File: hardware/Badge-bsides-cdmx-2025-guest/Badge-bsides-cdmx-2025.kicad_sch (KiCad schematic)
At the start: 30 parts, among them J1 SWDIO, J3 ADDON, J4 Conn_01x04_Pin, J5 I2C, J6 Conn_01x04_Pin, P6 USB_C_Plug_USB2.0, Q3 DMG3415U-7, SW11 ON, SW2 RESET, U1 PY32F030F28U6TR, U6 AP2112K-3.3

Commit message: feat(Hw):started_routing
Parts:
- added C67, C68, C69, C70: 10uF, Capacitor_SMD:C_0603_1608Metric, symbol Device:C_Small
- added R5, R6, R7, R8: 10k, Resistor_SMD:R_0603_1608Metric, symbol Device:R_Small
- added SW10, SW7, SW8, SW9: SW_Push, Footprints:TS1088R02026, symbol Switch:SW_Push
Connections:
- net +3.3V: no longer BT3.2 (+)
- net +3V3: now also R5.2, R6.2, R7.2, R8.2
- net +BATT: now also BT3.2 (+)
- net GND: now also C67.2, C68.2, C69.2, C70.2, SW10.1, SW7.1, SW8.1, SW9.1
- net GPIO1: now also J3.6 (Pin_6), U1.3 (PA7); no longer J3.5 (Pin_5), U1.17 (PA1)
- net GPIO2: now also J3.5 (Pin_5), U1.5 (PA12); no longer J3.6 (Pin_6), U1.16 (PA0)
- net LED1: now also U1.10 (PB6); no longer U1.2 (PA6)
- net LED2: now also U1.20 (PA4); no longer U1.3 (PA7)
- net BTTN2: now reaches U1.1 (PA5)
- net BTTN2: now also C68.1, R6.1, SW9.2
- new net BTTN1: C67.1, R5.1, SW8.2, U1.2 (PA6)
- new net BTTN3: C69.1, R7.1, SW7.2, U1.17 (PA1)
- new net BTTN4: C70.1, R8.1, SW10.2, U1.16 (PA0)
- no-connect marks 9 -> 3
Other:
- moved on the sheet: BT3, BT4

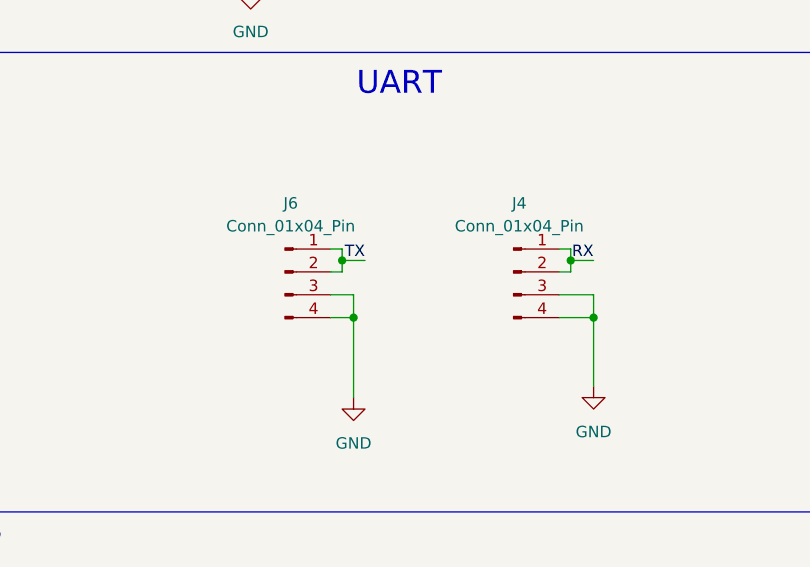
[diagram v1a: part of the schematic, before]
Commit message: feat(Hw):Route_Sponsor
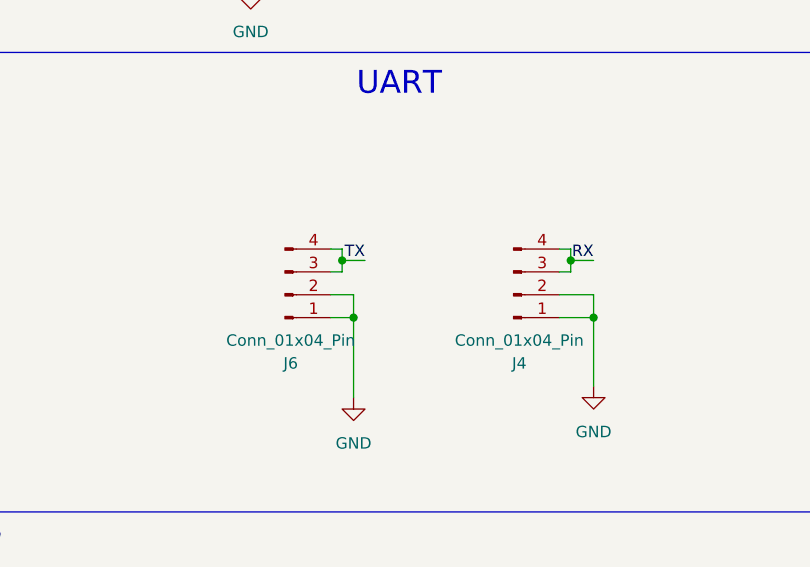
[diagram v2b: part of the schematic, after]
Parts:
- J4: footprint Connector_PinHeader_2.54mm:PinHeader_1x04_P2.54mm_Vertical -> Connector_PinHeader_2.54mm:PinHeader_1x04_P2.54mm_Horizontal
- J6: footprint Connector_PinHeader_2.54mm:PinHeader_1x04_P2.54mm_Vertical -> Connector_PinSocket_2.54mm:PinSocket_1x04_P2.54mm_Horizontal
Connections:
- net GND: now also J4.1 (Pin_1), J4.2 (Pin_2), J6.1 (Pin_1), J6.2 (Pin_2); no longer J4.3 (Pin_3), J4.4 (Pin_4), J6.3 (Pin_3), J6.4 (Pin_4)
- net RX: now also J4.3 (Pin_3), J4.4 (Pin_4); no longer J4.1 (Pin_1), J4.2 (Pin_2)
- net TX: now also J6.3 (Pin_3), J6.4 (Pin_4); no longer J6.1 (Pin_1), J6.2 (Pin_2)
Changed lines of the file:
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@@
 	(symbol
 		(lib_id "Connector:Conn_01x04_Pin")
-		(at 246.38 93.98 0)
-		(unit 1)
-		(exclude_from_sim no)
-		(in_bom yes)
-		(on_board yes)
-		(dnp no)
-		(fields_autoplaced yes)
+		(at 246.38 96.52 0)
+		(mirror x)
+		(unit 1)
+		(exclude_from_sim no)
+		(in_bom yes)
+		(on_board yes)
+		(dnp no)
 		(property "Reference" "J4"
-			(at 247.015 86.36 0)
+			(at 247.015 104.14 0)
 			(effects
 				(font
@@
 		)
 		(property "Value" "Conn_01x04_Pin"
-			(at 247.015 88.9 0)
-			(effects
-				(font
-					(size 1.27 1.27)
-				)
-			)
-		)
-		(property "Footprint" "Connector_PinHeader_2.54mm:PinHeader_1x04_P2.54mm_Vertical"
-			(at 246.38 93.98 0)
+			(at 247.015 101.6 0)
+			(effects
+				(font
+					(size 1.27 1.27)
+				)
+			)
+		)
+		(property "Footprint" "Connector_PinHeader_2.54mm:PinHeader_1x04_P2.54mm_Horizontal"
+			(at 246.38 96.52 0)
 			(effects
 				(font
@@
 		)
 		(property "Datasheet" "~"
-			(at 246.38 93.98 0)
+			(at 246.38 96.52 0)
 			(effects
 				(font
@@
 		)
 		(property "Description" "Generic connector, single row, 01x04, script generated"
-			(at 246.38 93.98 0)
+			(at 246.38 96.52 0)
 			(effects
 				(font
@@
 	(symbol
 		(lib_id "Connector:Conn_01x04_Pin")
-		(at 220.98 93.98 0)
-		(unit 1)
-		(exclude_from_sim no)
-		(in_bom yes)
-		(on_board yes)
-		(dnp no)
-		(fields_autoplaced yes)
+		(at 220.98 96.52 0)
+		(mirror x)
+		(unit 1)
+		(exclude_from_sim no)
+		(in_bom yes)
+		(on_board yes)
+		(dnp no)
 		(property "Reference" "J6"
-			(at 221.615 86.36 0)
+			(at 221.615 104.14 0)
 			(effects
 				(font
@@
 		)
 		(property "Value" "Conn_01x04_Pin"
-			(at 221.615 88.9 0)
-			(effects
-				(font
-					(size 1.27 1.27)
-				)
-			)
-		)
-		(property "Footprint" "Connector_PinHeader_2.54mm:PinHeader_1x04_P2.54mm_Vertical"
-			(at 220.98 93.98 0)
+			(at 221.615 101.6 0)
+			(effects
+				(font
+					(size 1.27 1.27)
+				)
+			)
+		)
+		(property "Footprint" "Connector_PinSocket_2.54mm:PinSocket_1x04_P2.54mm_Horizontal"
+			(at 220.98 96.52 0)
 			(effects
 				(font
@@
 		)
 		(property "Datasheet" "~"
-			(at 220.98 93.98 0)
+			(at 220.98 96.52 0)
 			(effects
 				(font
@@
 		)
 		(property "Description" "Generic connector, single row, 01x04, script generated"
-			(at 220.98 93.98 0)
-			(effects
-				(font
+			(at 220.98 96.52 0)
+			(effects
+				(font

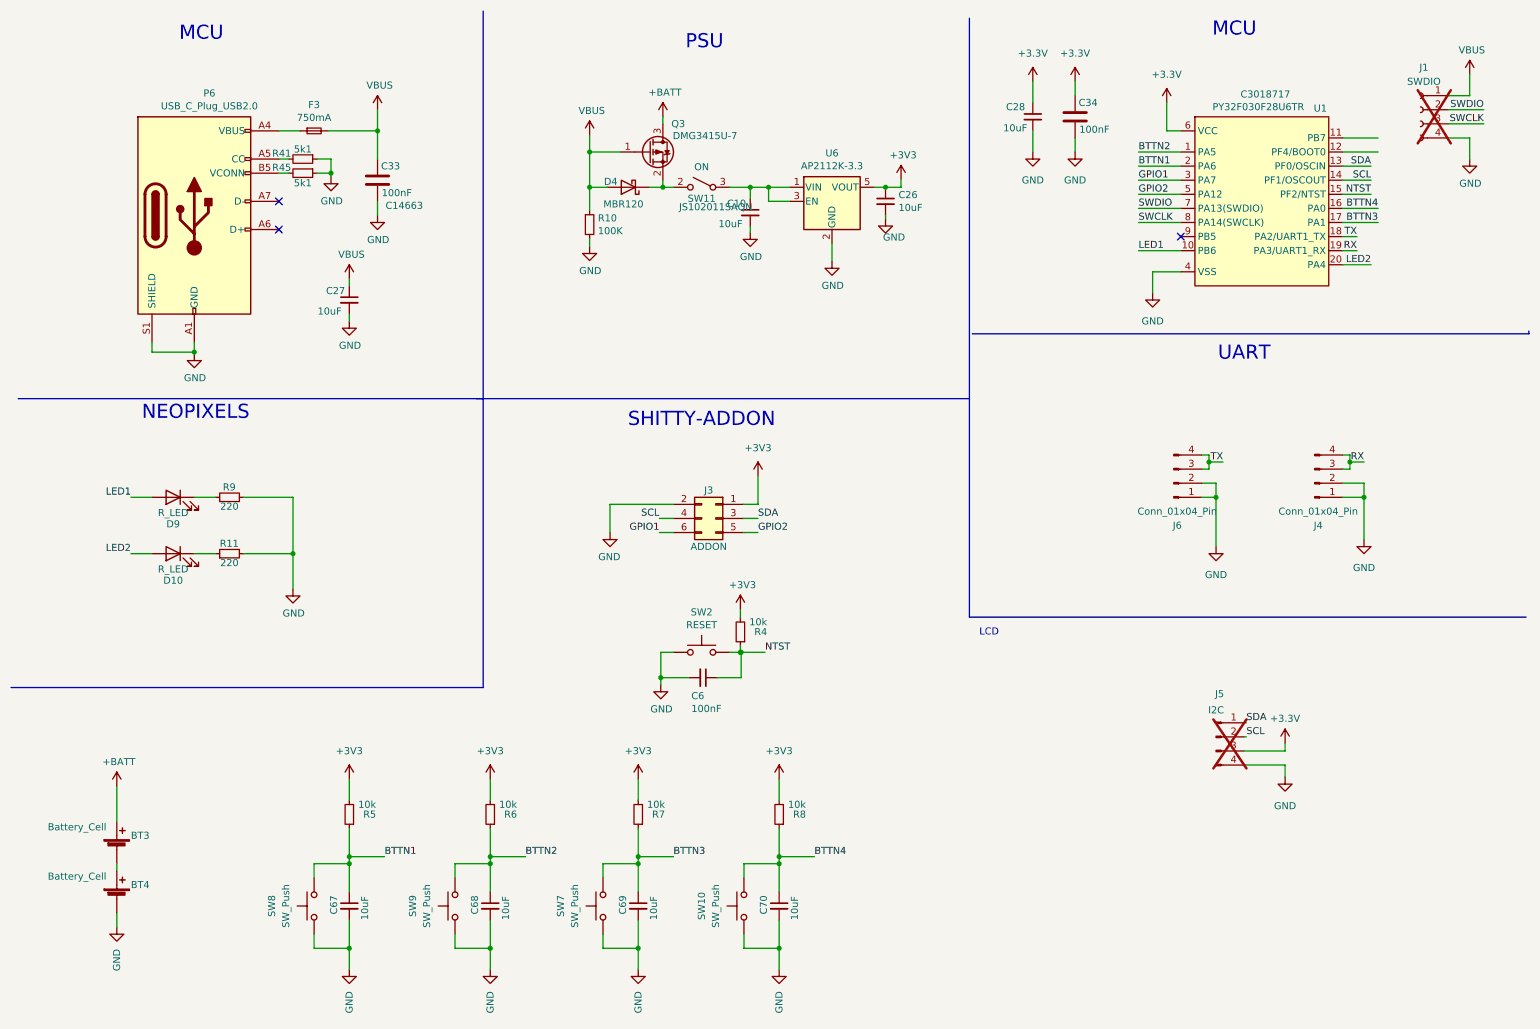
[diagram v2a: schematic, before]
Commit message: feat(Hw):Neopixels_added(sponsor)
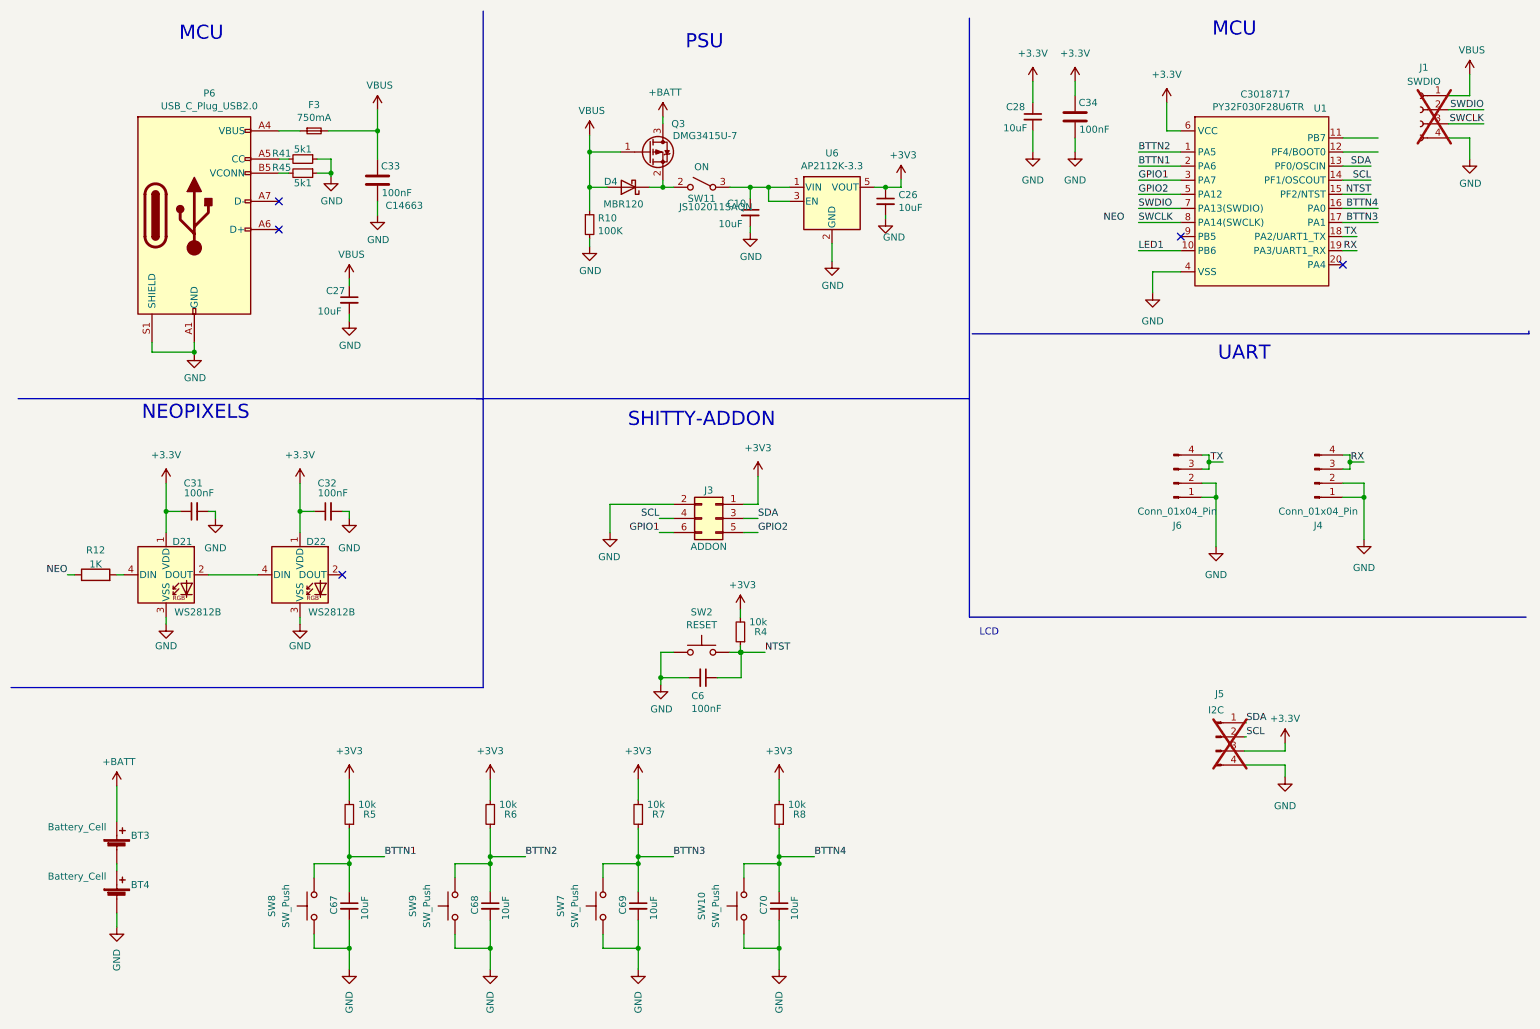
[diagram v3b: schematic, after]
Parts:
- removed D10, D9: R_LED, Footprints:LYT77K-K2M1, symbol Device:LED
- removed R11, R9: 220, Resistor_SMD:R_0603_1608Metric, symbol Device:R_Small
- added C31, C32: 100nF, Capacitor_SMD:C_0603_1608Metric, symbol Device:C_Small
- added D21, D22: WS2812B, Footprints:LED_SK6812-E, symbol LED:WS2812B
- added R12: 1K, Resistor_SMD:R_0603_1608Metric, symbol Device:R
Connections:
- net +3.3V: now also C31.1, C32.1, D21.1 (VDD), D22.1 (VDD)
- net GND: now also C31.2, C32.2, D21.3 (VSS), D22.3 (VSS)
- net LED2: no longer names the net of U1.20 (PA4)
- new net: D21.2 (DOUT), D22.4 (DIN)
- new net: D21.4 (DIN), R12.2
- new net NEO: R12.1
- no-connect marks 3 -> 5

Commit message: Feat(Hw): Fixed_Bom(Sponsor,guest)
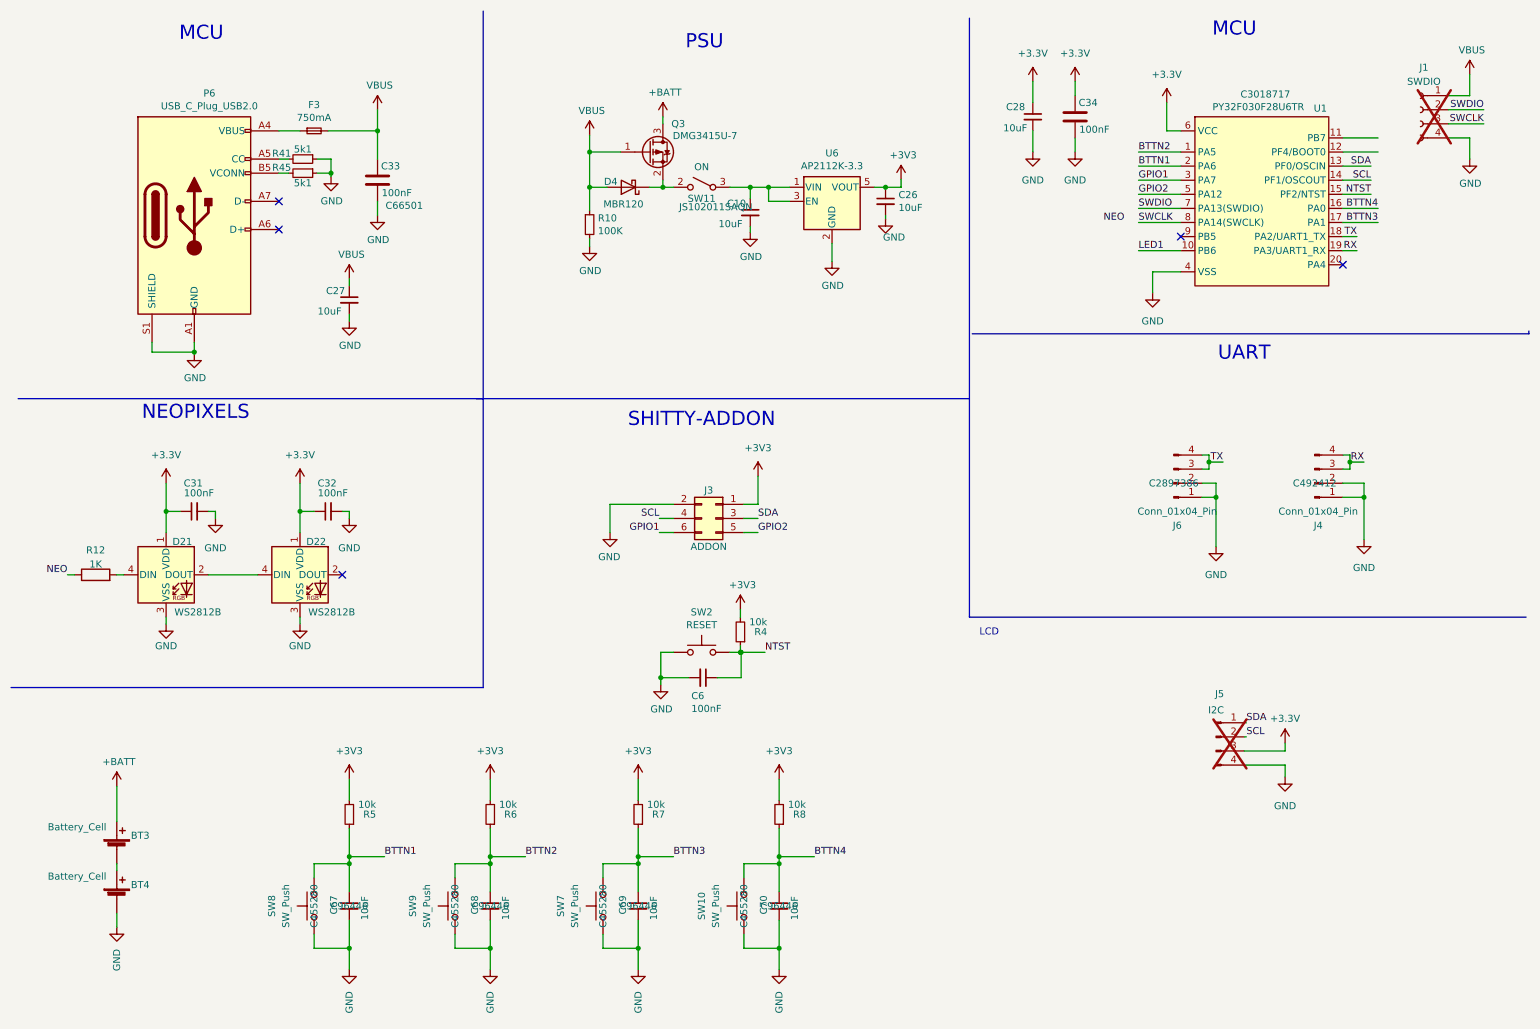
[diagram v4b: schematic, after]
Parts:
- C10, C26, C28: LCSC# C85713 -> C96446
- C31, C32: LCSC# C478888 -> C66501
- C33, C34: LCSC# C14663 -> C66501
- C67, C68, C69, C70: #LCSC C96446 -> (none); LCSC# (none) -> C96446
- J4: LCSC# (none) -> C492412
- J6: LCSC# (none) -> C2897386
- SW10, SW7, SW8, SW9: #LCSC C455280 -> (none); LCSC# (none) -> C455280
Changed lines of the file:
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@@
 			)
 		)
+		(property "LCSC#" "C492412"
+			(at 246.38 96.52 0)
+			(effects
+				(font
+					(size 1.27 1.27)
+				)
+			)
+		)
 		(pin "4"
 		)
@@
 			)
 		)
-		(property "LCSC#" "C478888"
+		(property "LCSC#" "C66501"
 			(at 68.58 101.6 0)
 			(effects
@@
 			)
 		)
-		(property "LCSC#" "C85713"
+		(property "LCSC#" "C96446"
 			(at 195.58 30.48 0)
 			(effects
@@
 			)
 		)
-		(property "LCSC#" "C85713"
+		(property "LCSC#" "C96446"
 			(at 144.653 47.752 0)
 			(effects
@@
 			)
 		)
-		(property "#LCSC" "C455280"
+		(property "#LCSC" ""
 			(at 143.51 172.72 0)
 			(effects
@@
 			)
 		)
+		(property "LCSC#" "C455280"
+			(at 143.51 172.72 0)
+			(effects
+				(font
+					(size 1.27 1.27)
+				)
+			)
+		)
 		(pin "2"
 		)
@@
 			)
 		)
-		(property "LCSC#" "C85713"
+		(property "LCSC#" "C96446"
 			(at 169.037 45.72 0)
 			(effects
@@
 			)
 		)
-		(property "#LCSC" "C96446"
+		(property "#LCSC" ""
 			(at 97.79 172.72 0)
 			(effects
@@
 			)
 		)
+		(property "LCSC#" "C96446"
+			(at 97.79 172.72 0)
+			(effects
+				(font
+					(size 1.27 1.27)
+				)
+			)
+		)
 		(pin "2"
 		)
@@
 			)
 		)
+		(property "LCSC#" "C2897386"
+			(at 220.98 96.52 0)
+			(effects
+				(font
+					(size 1.27 1.27)
+				)
+			)
+		)
 		(pin "4"
 		)
@@
 			)
 		)
-		(property "#LCSC" "C96446"
+		(property "#LCSC" ""
 			(at 72.39 172.72 0)
 			(effects
@@
 			)
 		)
+		(property "LCSC#" "C96446"
+			(at 72.39 172.72 0)
+			(effects
+				(font
+					(size 1.27 1.27)
+				)
+			)
+		)
 		(pin "2"
 		)
@@
 			)
 		)
-		(property "#LCSC" "C96446"
+		(property "#LCSC" ""
 			(at 149.86 172.72 0)
 			(effects
@@
 			)
 		)
+		(property "LCSC#" "C96446"
+			(at 149.86 172.72 0)
+			(effects
+				(font
+					(size 1.27 1.27)
+				)
+			)
+		)
 		(pin "2"
 		)
@@
 			)
 		)
-		(property "LCSC#" "C478888"
+		(property "LCSC#" "C66501"
 			(at 44.45 101.6 0)
 			(effects
@@
 			)
 		)
-		(property "#LCSC" "C455280"
+		(property "#LCSC" ""
 			(at 66.04 172.72 0)
 			(effects
@@
 			)
 		)
+		(property "LCSC#" "C455280"
+			(at 66.04 172.72 0)
+			(effects
+				(font
+					(size 1.27 1.27)
+				)
+			)
+		)
 		(pin "2"
 		)
@@
 			)
 		)
-		(property "LCSC#" "C14663"
+		(property "LCSC#" "C66501"
 			(at 209.296 30.48 0)
 			(effects
@@
 			)
 		)
-		(property "#LCSC" "C455280"
+		(property "#LCSC" ""
 			(at 118.11 172.72 0)
 			(effects
@@
 			)
 		)
+		(property "LCSC#" "C455280"
+			(at 118.11 172.72 0)
+			(effects
+				(font
+					(size 1.27 1.27)
+				)
+			)
+		)
 		(pin "2"
 		)
@@
 			)
 		)
-		(property "#LCSC" "C96446"
+		(property "#LCSC" ""
 			(at 124.46 172.72 0)
 			(effects
@@
 			)
 		)
+		(property "LCSC#" "C96446"
+			(at 124.46 172.72 0)
+			(effects
+				(font
+					(size 1.27 1.27)
+				)
+			)
+		)
 		(pin "2"
 		)
@@
 			)
 		)
-		(property "LCSC#" "C14663"
+		(property "LCSC#" "C66501"
 			(at 82.296 46.482 0)
 			(effects
@@
 			)
 		)
-		(property "#LCSC" "C455280"
+		(property "#LCSC" ""
 			(at 91.44 172.72 0)
 			(effects
@@
 			(at 91.44 172.72 0)
 			(effects
+				(font
+					(size 1.27 1.27)
+				)
+			)
+		)
+		(property "LCSC#" "C455280"
+			(at 91.44 172.72 0)
+			(effects

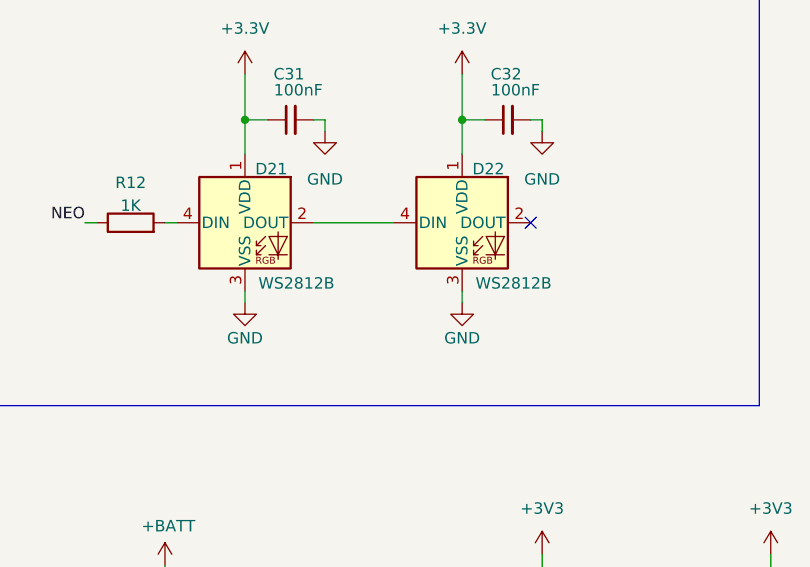
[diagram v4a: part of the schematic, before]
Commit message: Feat(Hw): FIxed_neopixels_bom(Sponsor,guest)
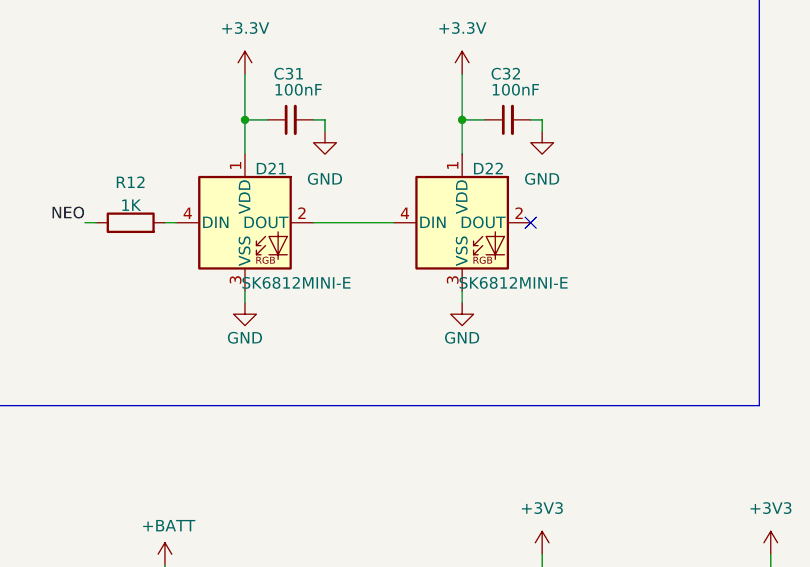
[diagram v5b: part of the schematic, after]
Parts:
- D21, D22: value WS2812B -> SK6812MINI-E; LCSC# C527089 -> C5149201
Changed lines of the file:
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@@
 			)
 		)
-		(property "Value" "WS2812B"
+		(property "Value" "SK6812MINI-E"
 			(at 45.085 119.761 0)
 			(effects
@@
 			)
 		)
-		(property "LCSC#" "C527089"
+		(property "LCSC#" "C5149201"
 			(at 39.37 113.03 0)
 			(effects
@@
 			)
 		)
-		(property "Value" "WS2812B"
+		(property "Value" "SK6812MINI-E"
 			(at 69.215 119.761 0)
 			(effects
@@
 			)
 		)
-		(property "LCSC#" "C527089"
+		(property "LCSC#" "C5149201"
 			(at 63.5 113.03 0)
 			(effects
